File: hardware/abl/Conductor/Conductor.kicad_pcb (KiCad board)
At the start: 2 copper layers, 53.5 x 29.1 mm, 6 parts, among them J1 009159008603906, J2 009159008603906

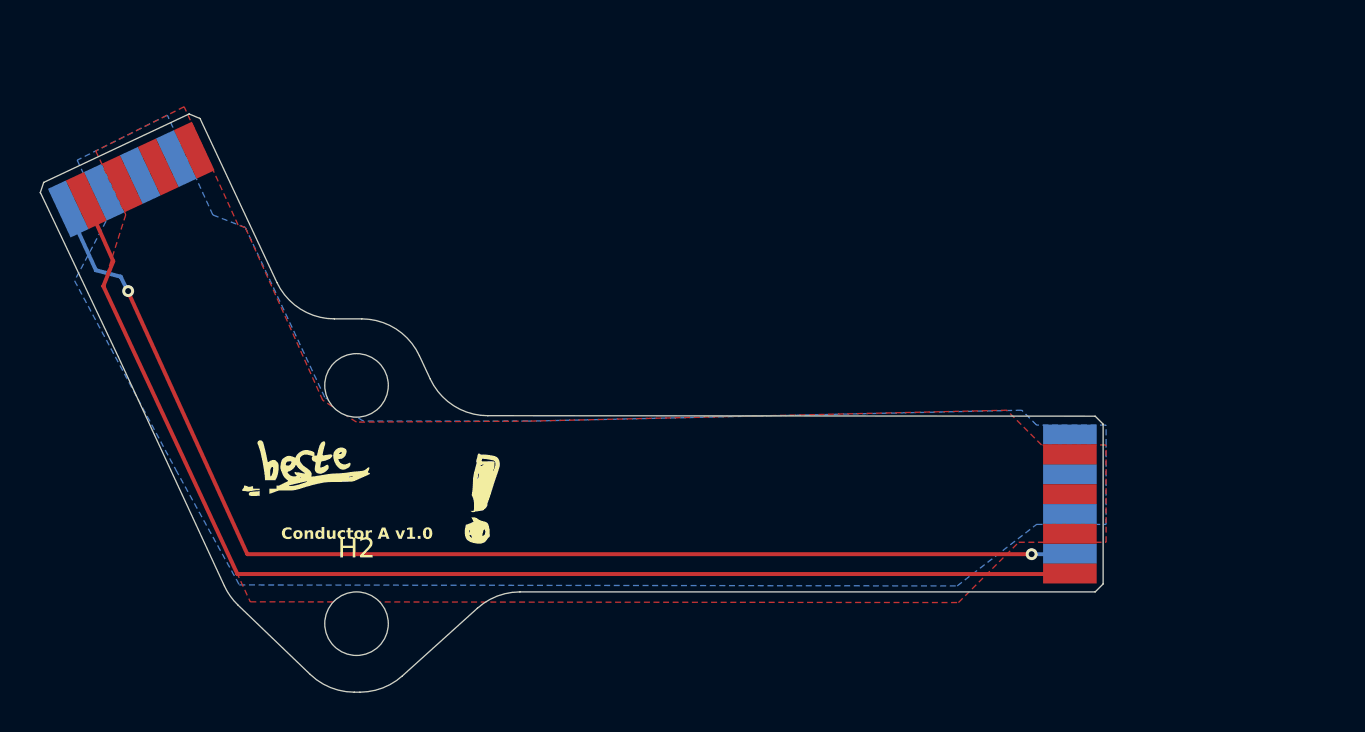
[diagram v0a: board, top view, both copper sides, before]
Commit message: Clean up schematics and minor fixes in PCB layouts.
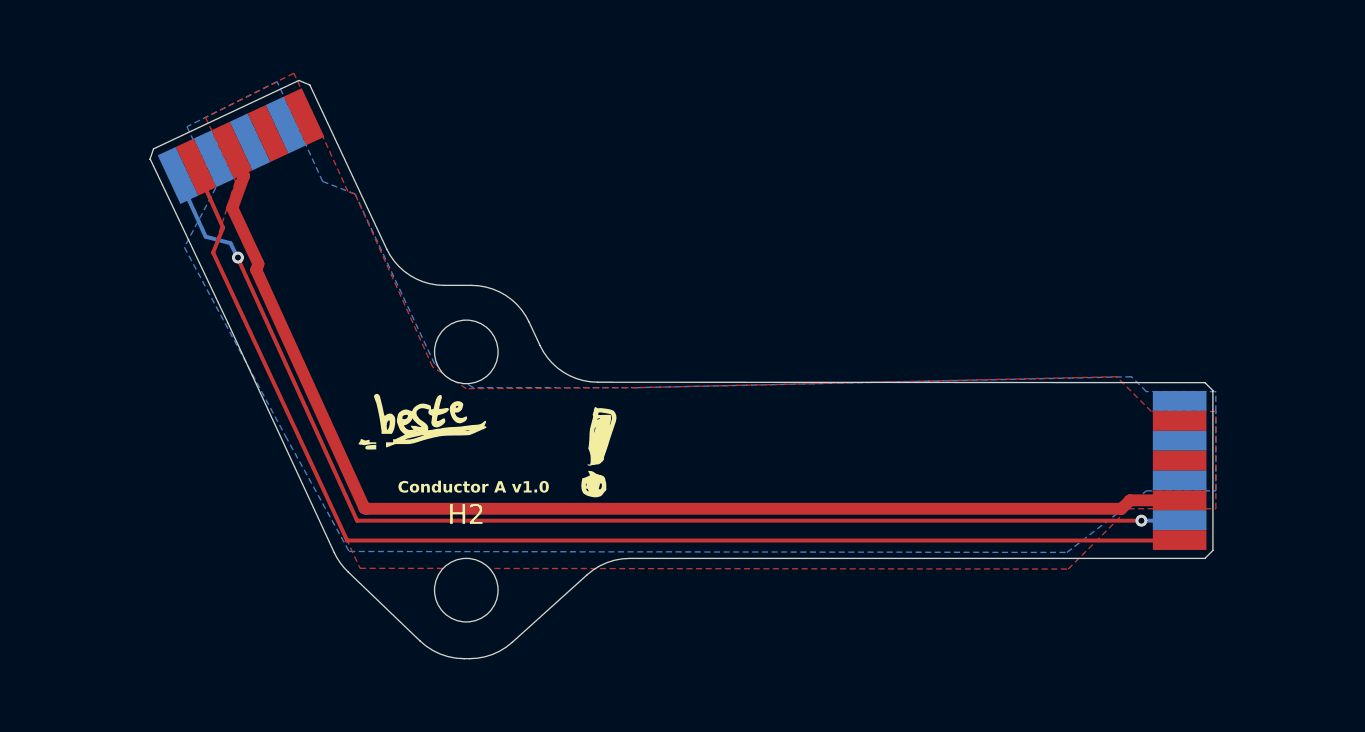
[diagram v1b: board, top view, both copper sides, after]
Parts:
- moved G*** 6.32 mm to (85.8, 89.7)
- moved G*** 6.32 mm to (85.4, 89.7)
- moved J2 5.78 mm to (70.1, 77.6)
- moved H1 5.78 mm to (84.5, 85.1)
- moved J1 5.78 mm to (119.1, 87.0)
- moved H2 5.78 mm to (84.5, 97.1)
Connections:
- J1 pad 6: /VLED -> /5V
- J2 pad 4: /VLED -> /5V
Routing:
- net /5V: track 0.00 -> 61.0 mm
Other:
- outline, holes or cut-outs redrawn

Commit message: Add "make first, break last" contacts to prevent latch-up when hot-plugging.
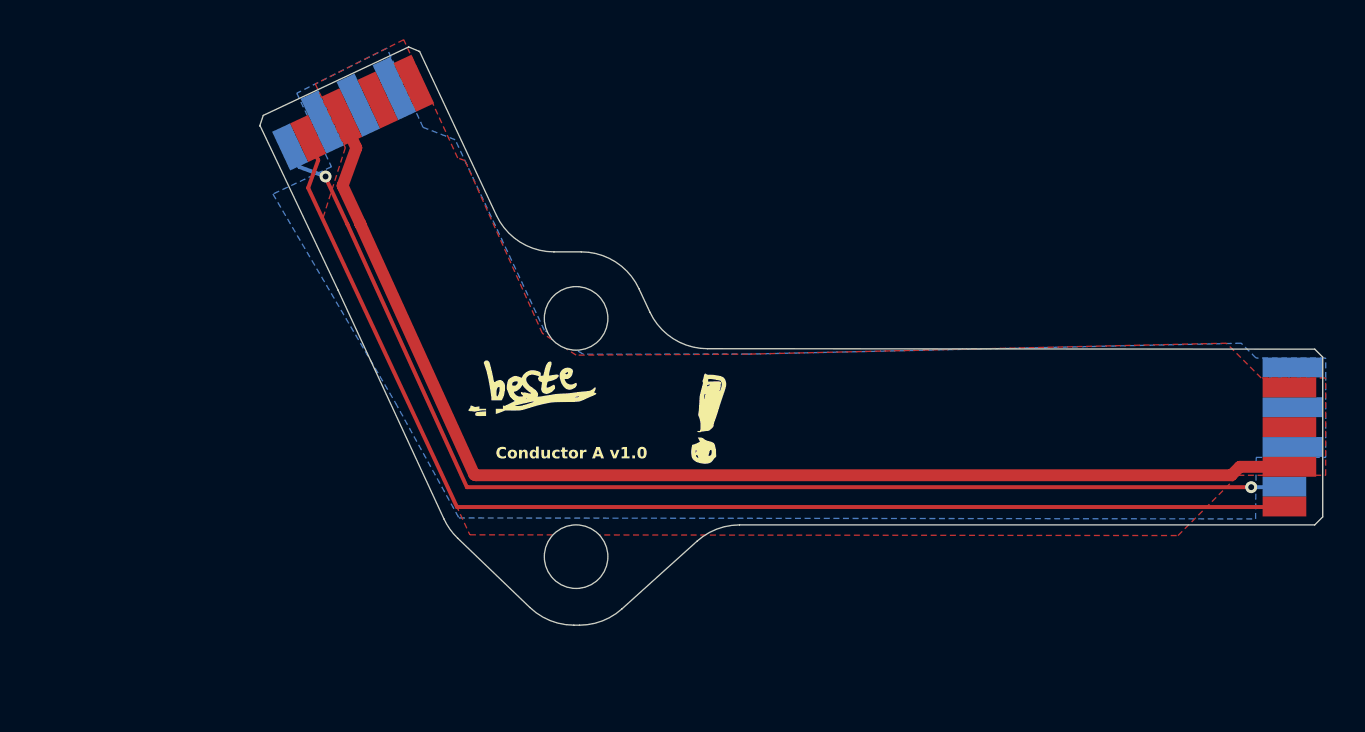
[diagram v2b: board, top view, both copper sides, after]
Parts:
- moved G*** 5.78 mm to (91.3, 88.0)
- moved H1 5.78 mm to (90.1, 83.4)
- moved J1 5.78 mm to (124.6, 85.4)
- moved J2 5.78 mm to (75.7, 75.9)
- moved H2 5.78 mm to (90.1, 95.4)
- moved G*** 5.78 mm to (90.9, 88.0)
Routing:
- net /SCL: track 55.0 -> 60.2 mm
